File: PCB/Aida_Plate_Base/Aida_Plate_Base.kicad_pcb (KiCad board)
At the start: 2 copper layers, 119.7 x 83.3 mm, 16 parts

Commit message: 右手パーツ配置中
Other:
- outline, holes or cut-outs redrawn
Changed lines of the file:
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@@
+		(layer "Edge.Cuts")
+	)
+	(gr_arc
+		(start 34.528103 97.631245)
+		(mid 32.002406 96.585067)
+		(end 30.956228 94.05937)
+		(stroke
+			(width 0.05)
+			(type default)
+		)
 		(layer "Edge.Cuts")
 	)
@@
 	)
 	(gr_line
-		(start 66.67506 116.681247)
+		(start 66.674978 116.681245)
 		(end 148.232943 116.681318)
 		(stroke
@@
 		(layer "Edge.Cuts")
 	)
+	(gr_arc
+		(start 150.614193 114.300102)
+		(mid 149.916733 115.983892)
+		(end 148.232943 116.681352)
+		(stroke
+			(width 0.05)
+			(type default)
+		)
+		(layer "Edge.Cuts")
+	)
 	(gr_curve
 		(pts
@@
 	)
 	(gr_arc
-		(start 66.67506 116.681336)
-		(mid 64.570312 115.809521)
-		(end 63.698497 113.704773)
-		(stroke
-			(width 0.05)
-			(type default)
-		)
-		(layer "Edge.Cuts")
-	)
-	(gr_arc
 		(start 150.01611 95.546185)
 		(mid 150.437031 95.720536)
@@
 	(gr_curve
 		(pts
-			(xy 30.95625 92.86875) (xy 30.95625 95.25) (xy 30.95625 97.63125) (xy 35.71875 97.63125)
-		)
-		(stroke
-			(width 0.05)
-			(type default)
-		)
-		(layer "Edge.Cuts")
-	)
-	(gr_curve
-		(pts
 			(xy 31.551593 73.818874) (xy 30.95625 76.2) (xy 30.95625 77.390625) (xy 30.95625 78.58125)
 		)
@@
 	)
 	(gr_arc
+		(start 66.674978 116.681245)
+		(mid 64.149281 115.635067)
+		(end 63.103103 113.10937)
+		(stroke
+			(width 0.05)
+			(type default)
+		)
+		(layer "Edge.Cuts")
+	)
+	(gr_arc
 		(start 118.16755 57.446954)
 		(mid 118.588471 57.621305)
@@
 		(layer "Edge.Cuts")
 	)
-	(gr_curve
-		(pts
-			(xy 35.71875 97.63125) (xy 63.698495 97.63125) (xy 63.698495 97.63132) (xy 63.698495 113.704773)
-		)
-		(stroke
-			(width 0.05)
-			(type default)
-		)
-		(layer "Edge.Cuts")
-	)
 	(gr_line
 		(start 128.287639 77.095519)
@@
 		(layer "Edge.Cuts")
 	)
+	(gr_arc
+		(start 59.531228 97.631245)
+		(mid 62.056925 98.677423)
+		(end 63.103103 101.20312)
+		(stroke
+			(width 0.05)
+			(type default)
+		)
+		(layer "Edge.Cuts")
+	)
+	(gr_line
+		(start 34.528103 97.631245)
+		(end 59.531228 97.631245)
+		(stroke
+			(width 0.05)
+			(type default)
+		)
+		(layer "Edge.Cuts")
+	)
 	(gr_line
 		(start 99.71325 33.932566)
@@
 	)
 	(gr_line
+		(start 63.103103 101.20312)
+		(end 63.103103 113.10937)
+		(stroke
+			(width 0.05)
+			(type default)
+		)
+		(layer "Edge.Cuts")
+	)
+	(gr_line
 		(start 30.95625 78.58125)
-		(end 30.95625 92.86875)
+		(end 30.95625 94.059375)
 		(stroke
 			(width 0.05)
@@
 		(start 150.614193 114.300102)
 		(end 150.611353 96.14145)
-		(stroke
-			(width 0.05)
-			(type default)
-		)
-		(layer "Edge.Cuts")
-	)
-	(gr_arc
-		(start 150.614193 114.300068)
-		(mid 149.916755 115.983902)
-		(end 148.232943 116.681318)
 		(stroke
 			(width 0.05)
@@
 	(group ""
 		(members "0d3ae00c-38f9-41fb-9129-45fe07cda796" "13ff7425-956b-434e-8584-2c0b4094a7a6"
-			"1b0ccb9a-d96e-4782-a512-c9f605249095" "20c02181-cdd8-4e1b-923b-844417615a0d"
-			"2554f8dd-7a6c-488f-929c-c946b621c0c9" "299285bc-f532-42d0-bf1f-bdc65c39bc74"
-			"312757f6-8a43-47db-ad6d-c7b72317d031" "35afd5c6-b9ef-4eb2-93fe-0eb114a61daa"
-			"361405b5-d627-4fe6-90d4-e03f60a64640" "4a474e13-4704-4f1f-936c-faf10c74802c"
+			"17a05441-9ecf-4ae5-8ac7-61cf64818c61" "1b0ccb9a-d96e-4782-a512-c9f605249095"
+			"20c02181-cdd8-4e1b-923b-844417615a0d" "2554f8dd-7a6c-488f-929c-c946b621c0c9"
+			"299285bc-f532-42d0-bf1f-bdc65c39bc74" "312757f6-8a43-47db-ad6d-c7b72317d031"
+			"35afd5c6-b9ef-4eb2-93fe-0eb114a61daa" "361405b5-d627-4fe6-90d4-e03f60a64640"
+			"457b6ade-6a3b-4925-8480-04768d7b5cf7" "4a474e13-4704-4f1f-936c-faf10c74802c"
 			"647eddda-5685-4036-8dde-290bb8f2a5ab" "6bfe3497-7358-468a-9d29-3ca56a585085"
-			"73f33da1-786f-4266-ab60-9ff4686f405d" "768c5e63-1218-4ba3-9532-4c9e73a447d1"
-			"839919dc-e7c6-4a2f-8c3c-902a59ca1fef" "8dd19543-b4d3-4d5a-8658-7678d8e65cfc"
-			"98c5fd14-f64b-4193-9675-4d46ddb228a5" "99c26ef8-0620-4134-8579-c78cd2cfbb08"
+			"768c5e63-1218-4ba3-9532-4c9e73a447d1" "839919dc-e7c6-4a2f-8c3c-902a59ca1fef"
+			"8dd19543-b4d3-4d5a-8658-7678d8e65cfc" "99c26ef8-0620-4134-8579-c78cd2cfbb08"
 			"a07c95c3-ed9c-466a-a608-236f3fb7fbc3" "ac25fb71-ad69-4ab5-bf9e-9160d2f441d4"
-			"b18f0ba1-a030-4aa5-b65f-341f00f3e289" "c0b84a16-6586-467e-8f67-57e31c51926f"
+			"ae03513d-a603-467c-85eb-6ea9060efd5b" "b18f0ba1-a030-4aa5-b65f-341f00f3e289"
 			"c885e857-08ed-44ae-8c42-07f47adcd5c7" "cd18fae9-c54f-43c9-ac3b-43056f6c28ea"
-			"dba2909c-a281-408d-968f-2686105d6c50" "e48c187a-3416-4602-b05b-835df83f1cbf"
-			"f3ba118f-c368-4bea-bb07-88a11db42e95" "f4d8456d-3085-49d8-aab9-7582066fe261"
-		)
-	)
+			"d5e8377f-7056-4d30-93f7-f58e1f386200" "d88fe785-6251-4cc6-afd6-2c3672b32a10"
+			"dba2909c-a281-408d-968f-2686105d6c50" "e1afaae8-947b-4a02-ab1b-9884809ac6bb"
+			"e48c187a-3416-4602-b05b-835df83f1cbf" "f3ba118f-c368-4bea-bb07-88a11db42e95"
+		)
+	)

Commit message: 原点ガイドを追加。基板Mid_InsideのLED穴形状調整
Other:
- board text added: "Center Origin"
- board text added: "Grid Origin"
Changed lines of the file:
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@@
 		(layer "Edge.Cuts")
+	)
+	(gr_line
+		(start 23.8125 21.43125)
+		(end 23.8125 26.19375)
+		(stroke
+			(width 0.1)
+			(type default)
+		)
+		(layer "User.1")
+	)
+	(gr_line
+		(start 21.43125 23.8125)
+		(end 26.19375 23.8125)
+		(stroke
+			(width 0.1)
+			(type default)
+		)
+		(layer "User.1")
+	)
+	(gr_line
+		(start 152.4 21.43125)
+		(end 152.4 26.19375)
+		(stroke
+			(width 0.1)
+			(type default)
+		)
+		(layer "User.1")
+	)
+	(gr_line
+		(start 150.01875 23.8125)
+		(end 154.78125 23.8125)
+		(stroke
+			(width 0.1)
+			(type default)
+		)
+		(layer "User.1")
+	)
+	(gr_circle
+		(center 23.8125 23.8125)
+		(end 25.003125 23.8125)
+		(stroke
+			(width 0.1)
+			(type default)
+		)
+		(fill no)
+		(layer "User.1")
+	)
+	(gr_circle
+		(center 152.4 23.8125)
+		(end 153.590625 23.8125)
+		(stroke
+			(width 0.1)
+			(type default)
+		)
+		(fill no)
+		(layer "User.1")
 	)
 	(gr_text "#Aida_kbd DN0010 @jpskenn"
@@
 		(at 42.267197 32.1469 0)
 		(layer "Eco2.User")
+		(effects
+			(font
+				(size 1 1)
+				(thickness 0.15)
+			)
+			(justify left bottom)
+		)
+	)
+	(gr_text "Center Origin"
+		(at 148.828125 21.43125 0)
+		(layer "User.1")
+		(effects
+			(font
+				(size 1 1)
+				(thickness 0.15)
+			)
+			(justify left bottom)
+		)
+	)
+	(gr_text "Grid Origin"
+		(at 20.240625 21.43125 0)
+		(layer "User.1")
 		(effects
 			(font
@@
 		)
 	)
+	(group ""
+		(members "068ae3cc-dcc8-43bd-bf5f-1b93a4434401" "354e347a-35aa-4468-a537-7bcd2d99042b"
+			"4140c550-8577-45be-a45b-0aba58c9eaf4" "aa6b5bf3-fc6e-4142-9bc7-bba26cdac934"
+		)
+	)
+	(group ""
+		(members "0dad3f82-d388-4956-9e06-65bf1ddc078e" "66a08e28-629b-4872-a554-3d2d82884515"
+			"6e5c0f5d-1d96-4f0c-8f28-8ce37dcb62e7" "dbaee11c-4ea8-4e77-9308-1c9ca9bcae6a"
+		)
+	)

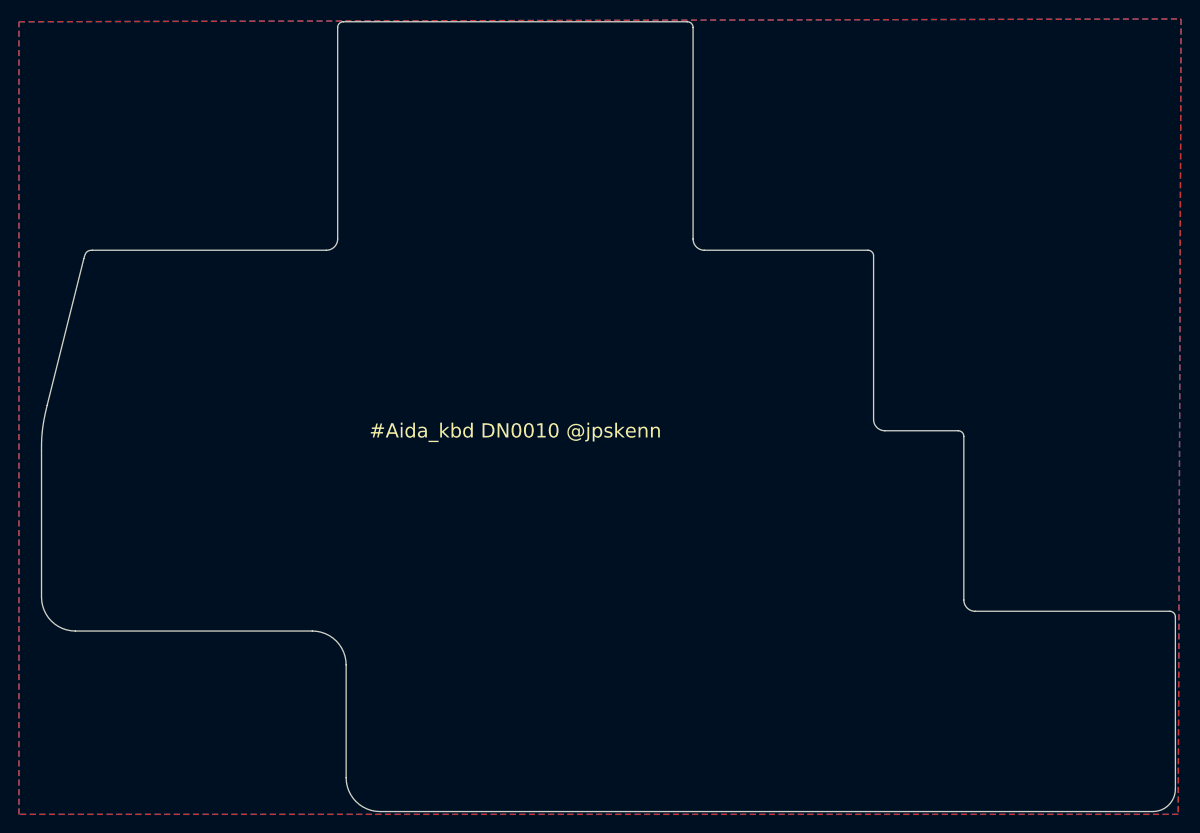
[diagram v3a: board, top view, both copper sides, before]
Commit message: LEDを1/16u下へ移動。 右手のフラッシュメモリとの干渉回避のためボトムプレートの穴位置調整。
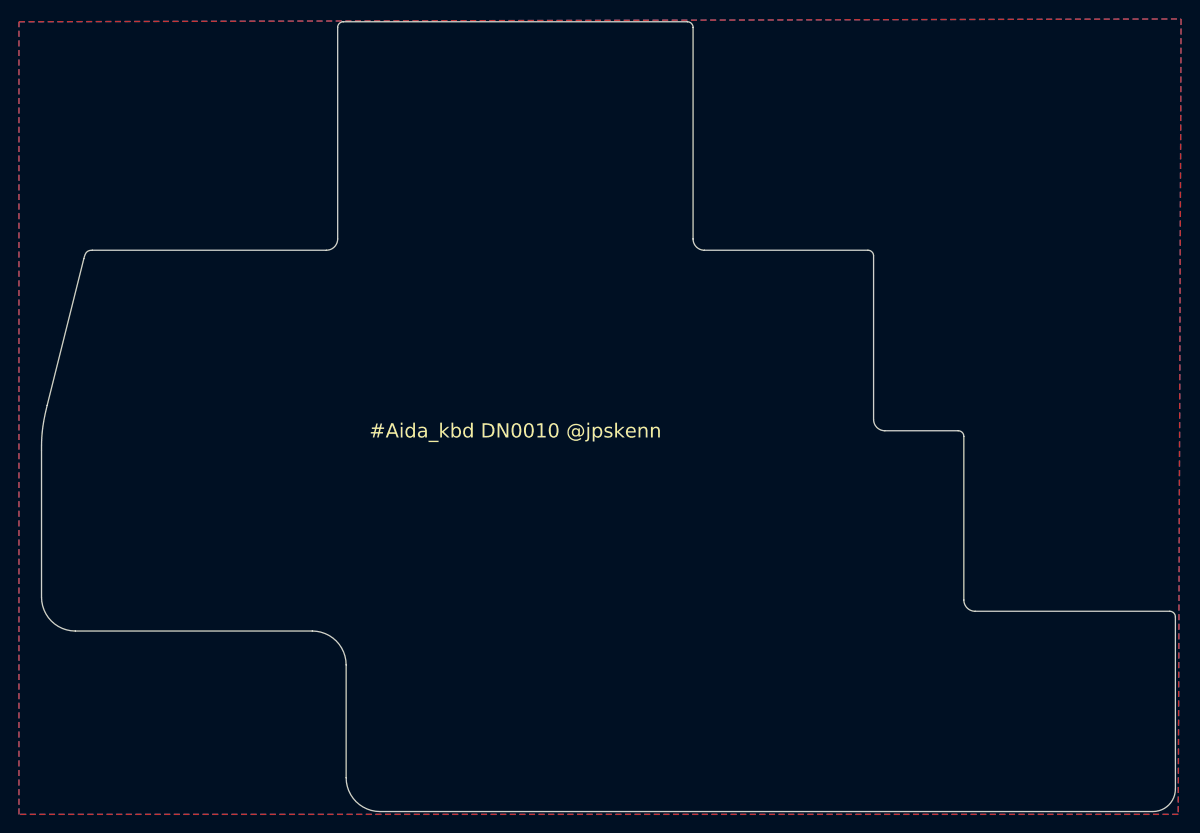
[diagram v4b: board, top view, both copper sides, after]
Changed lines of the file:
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@@
 	(gr_line
 		(start 118.16755 57.446954)
-		(end 100.903838 57.44695)
+		(end 100.903838 57.446878)
 		(stroke
 			(width 0.05)
@@
 	(gr_line
 		(start 35.42085 58.3399)
-		(end 31.550399 73.818606)
+		(end 31.551593 73.818874)
 		(stroke
 			(width 0.05)
@@
 	)
 	(gr_line
-		(start 61.010535 57.44695)
+		(start 61.01875 57.44695)
 		(end 36.3138 57.44695)
 		(stroke
@@
 	(gr_line
 		(start 66.674978 116.681245)
-		(end 148.232943 116.681318)
+		(end 148.232943 116.681352)
 		(stroke
 			(width 0.05)
@@
 	)
 	(gr_line
-		(start 118.762839 58.039413)
-		(end 118.76285 75.3059)
+		(start 118.762839 58.042219)
+		(end 118.76285 75.306022)
 		(stroke
 			(width 0.05)
@@
 	)
 	(gr_line
-		(start 150.0161 95.546185)
-		(end 129.47825 95.54615)
-		(stroke
-			(width 0.05)
-			(type default)
-		)
-		(layer "Edge.Cuts")
-	)
-	(gr_line
-		(start 99.11795 33.337517)
+		(start 150.01611 95.546185)
+		(end 129.478238 95.546078)
+		(stroke
+			(width 0.05)
+			(type default)
+		)
+		(layer "Edge.Cuts")
+	)
+	(gr_line
+		(start 99.11796 33.337301)
 		(end 62.80465 33.337513)
 		(stroke
@@
 	)
 	(gr_line
-		(start 127.6923 76.496554)
-		(end 119.953399 76.49655)
-		(stroke
-			(width 0.05)
-			(type default)
-		)
-		(layer "Edge.Cuts")
-	)
-	(gr_line
-		(start 62.209278 33.932802)
+		(start 127.69235 76.49655)
+		(end 119.953438 76.49655)
+		(stroke
+			(width 0.05)
+			(type default)
+		)
+		(layer "Edge.Cuts")
+	)
+	(gr_line
+		(start 62.209385 33.932802)
 		(end 62.209278 56.256362)
 		(stroke
@@
 	)
 	(gr_line
-		(start 128.287639 77.095519)
+		(start 128.287639 77.091815)
 		(end 128.28765 94.35555)
 		(stroke
@@
 	)
 	(gr_line
-		(start 99.71325 33.932566)
+		(start 99.713249 33.932566)
 		(end 99.71325 56.25635)
 		(stroke
@@
 	(gr_line
 		(start 30.95625 78.58125)
-		(end 30.95625 94.059375)
-		(stroke
-			(width 0.05)
+		(end 30.956228 94.05937)
+		(stroke
+			(width 0.05)

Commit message: 製造用出力
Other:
- board text removed: "#Aida_kbd DN0010 @jpskenn"
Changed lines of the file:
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@@
 			(outputformat 1)
 			(mirror no)
-			(drillshape 1)
+			(drillshape 0)
 			(scaleselection 1)
-			(outputdirectory "")
+			(outputdirectory "Export/")
 		)
 	)
@@
 		(layer "User.1")
 	)
-	(gr_text "#Aida_kbd DN0010 @jpskenn"
-		(at 80.962548 77.39067 0)
-		(layer "F.SilkS")
-		(effects
-			(font
-				(size 1.5 1.5)
-				(thickness 0.1875)
-			)
-			(justify bottom)
-		)
-	)
 	(gr_text "Top PCB outline"
